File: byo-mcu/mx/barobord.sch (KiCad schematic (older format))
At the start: 134 parts, among them J1 Pimoroni, J2 Conn_01x02_Female, SW1 SW_Push, SW10 SW_Push, SW11 SW_Push, SW12 SW_Push, SW13 SW_Push, SW14 SW_Push, SW15 SW_Push, SW16 SW_Push, SW17 SW_Push, SW18 SW_Push, SW19 SW_Push, SW2 SW_Push, SW20 SW_Push, SW21 SW_Push, SW22 SW_Push, SW23 SW_Push, SW24 SW_Push, SW25 SW_Push, SW26 SW_Push, SW27 SW_Push, SW28 SW_Push, SW29 SW_Push, SW3 SW_Push, SW30 SW_Push, SW31 SW_Push, SW32 SW_Push, SW33 SW_Push, SW34 SW_Push, SW35 SW_Push, SW36 SW_Push, SW37 SW_Push, SW38 SW_Push, SW39 SW_Push, SW4 SW_Push, SW40 SW_Push, SW41 SW_Push, SW42 RotaryEncoder_Switch, SW43 RotaryEncoder_Switch, SW44 EVQWGD001, SW45 EVQWGD001, SW46 SW_DIP_x01, SW5 SW_Push, SW6 SW_Push, SW7 SW_Push, SW8 SW_Push, SW9 SW_Push, U1 Elite-C, U2 nice_nano

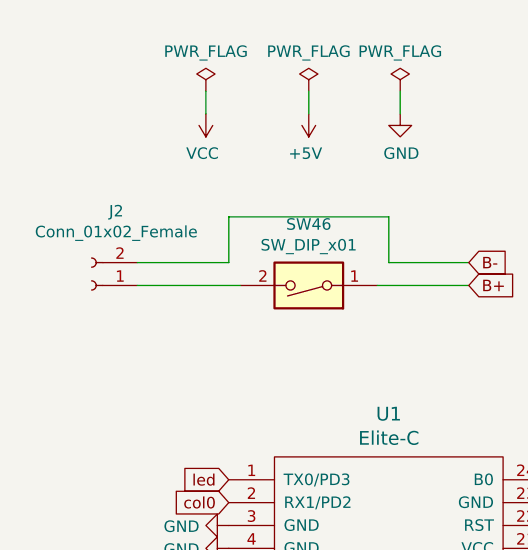
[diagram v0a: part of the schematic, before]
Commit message: converted jst connector from 2 pin to 3 pin to help prevent people from plugging in the battery backwards, and to support both wiring configurations for batteries
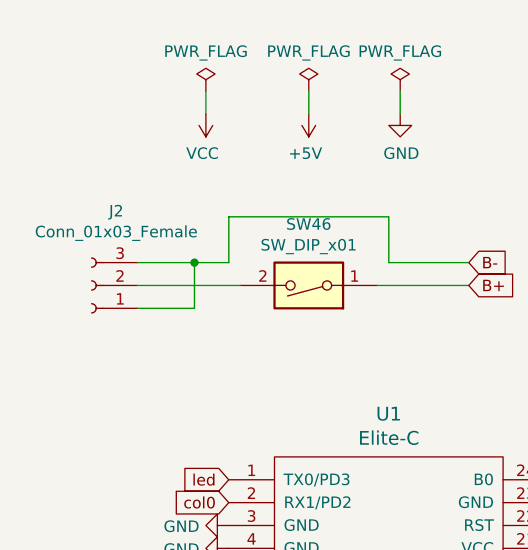
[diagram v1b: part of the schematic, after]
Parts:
- removed J2: Conn_01x02_Female, Connector_JST:JST_PH_S2B-PH-K_1x02_P2.00mm_Horizontal, symbol Connector:Conn_01x02_Female
- added J2: Conn_01x03_Female, Connector_JST:JST_PH_S3B-PH-K_1x03_P2.00mm_Horizontal, symbol Connector:Conn_01x03_Female
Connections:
- net B-: now also J2.1 (Pin_1), J2.3 (Pin_3)
- net at SW46.2: now also J2.2 (Pin_2)
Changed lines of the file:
@@
 B+
-$Comp
-L Connector:Conn_01x02_Female J2
-U 1 1 61AE01E2
-P 1150 1800
-F 0 "J2" H 1042 1475 50  0000 C CNN
-F 1 "Conn_01x02_Female" H 1042 1566 50  0000 C CNN
-F 2 "Connector_JST:JST_PH_S2B-PH-K_1x02_P2.00mm_Horizontal" H 1150 1800 50  0001 C CNN
-F 3 "~" H 1150 1800 50  0001 C CNN
-	1    1150 1800
-	-1   0    0    1
-$EndComp
 $Comp
 L Switch:SW_DIP_x01 SW46
@@
 B-
 Wire Wire Line
-	1350 1700 1750 1700
+	1350 1700 1600 1700
 Wire Wire Line
 	1750 1700 1750 1500
@@
 Wire Wire Line
 	1800 1800 1350 1800
+$Comp
+L Connector:Conn_01x03_Female J2
+U 1 1 61BEA860
+P 1150 1800
+F 0 "J2" H 1042 1475 50  0000 C CNN
+F 1 "Conn_01x03_Female" H 1042 1566 50  0000 C CNN
+F 2 "Connector_JST:JST_PH_S3B-PH-K_1x03_P2.00mm_Horizontal" H 1150 1800 50  0001 C CNN
+F 3 "~" H 1150 1800 50  0001 C CNN
+F 4 "C157929" H 1150 1800 50  0001 C CNN "LCSC"
+	1    1150 1800
+	-1   0    0    1
+$EndComp
+Wire Wire Line
+	1350 1900 1600 1900
+Wire Wire Line
+	1600 1900 1600 1700
+Connection ~ 1600 1700
+Wire Wire Line
+	1600 1700 1750 1700
 $EndSCHEMATC
